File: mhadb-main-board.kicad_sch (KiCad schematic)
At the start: 9 parts, among them U1 ESP32-S3FN8

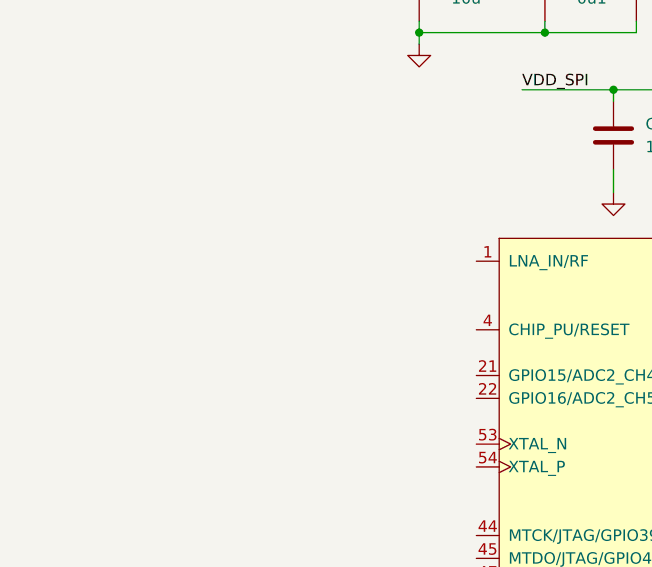
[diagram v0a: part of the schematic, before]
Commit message: schem: import 2.4GHZ rf circuit
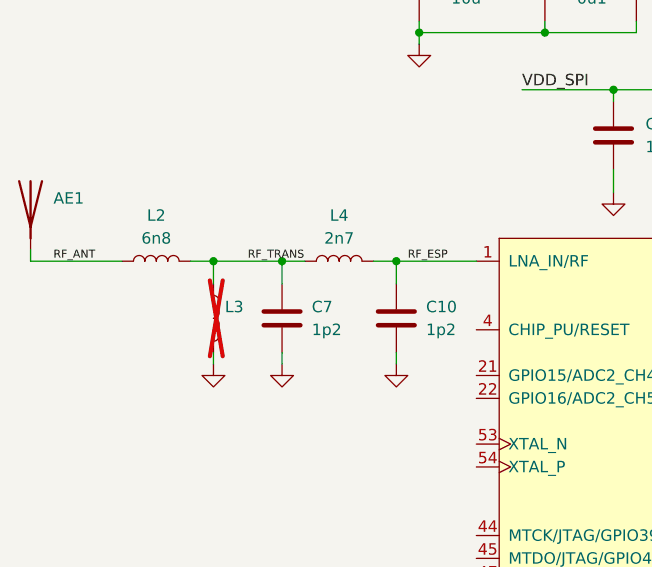
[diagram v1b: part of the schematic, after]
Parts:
- added AE1: Antenna, RF_Antenna:Johanson_2450AT18x100, symbol Device:Antenna
- added C10, C7: 1p2, Capacitor_SMD:C_0402_1005Metric, symbol Device:C
- added L2: 6n8, Inductor_SMD:L_0402_1005Metric, symbol Device:L
- added L3: L, Inductor_SMD:L_0402_1005Metric, symbol Device:L
- added L4: 2n7, Inductor_SMD:L_0402_1005Metric, symbol Device:L
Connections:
- net GND: now also C10.2, C7.2, L3.2
- net RF_ESP: now reaches U1.1 (LNA_IN/RF)
- net RF_ESP: now also C10.1, L4.2
- new net RF_ANT: AE1.1 (A), L2.1
- new net RF_TRANS: C7.1, L2.2, L3.1, L4.1

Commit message: schem: import reset circuit
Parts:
- added C1: 1u, Capacitor_SMD:C_0402_1005Metric, symbol Device:C
- added R1: 10k, Resistor_SMD:R_0402_1005Metric, symbol Device:R
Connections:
- net +3V3: now also R1.1
- net GND: now also C1.2
- net at U1.4 (CHIP_PU/RESET): now also C1.1, R1.2
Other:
- note added: "EN RC delay"
- moved on the sheet: AE1, C10, C7, L2, L3, L4

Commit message: schem: import HSE oscilator
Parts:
- added C2, C5: 12p, Capacitor_SMD:C_0402_1005Metric, symbol Device:C
- added L1: 24n, Inductor_SMD:L_0402_1005Metric, symbol Device:L
- added Y1: 48M, Crystal:Crystal_SMD_2016-4Pin_2.0x1.6mm, symbol Device:Crystal_GND24
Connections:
- net GND: now also C2.1, C5.2, Y1.2, Y1.4
- net XTAL_N: now reaches U1.53 (XTAL_N)
- net XTAL_N: now also C5.1, Y1.3
- net XTAL_P: now reaches U1.54 (XTAL_P)
- net XTAL_P: now also L1.1
- new net XTAL_PL: C2.2, L1.2, Y1.1
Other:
- note added: "HSE"

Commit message: schem: add BOOT pullup
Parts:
- added R9: 10k, Resistor_SMD:R_0402_1005Metric, symbol Device:R
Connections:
- net +3V3: now also R9.2
- net BOOT: now reaches U1.5 (GPIO0/BOOT)
- net BOOT: now also R9.1
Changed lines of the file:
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@@
 	(wire
 		(pts
+			(xy 240.03 73.66) (xy 245.11 73.66)
+		)
+		(stroke
+			(width 0)
+			(type default)
+		)
+	)
+	(wire
+		(pts
 			(xy 209.55 40.64) (xy 209.55 53.34)
 		)
@@
 	(wire
 		(pts
+			(xy 252.73 73.66) (xy 266.7 73.66)
+		)
+		(stroke
+			(width 0)
+			(type default)
+		)
+	)
+	(wire
+		(pts
 			(xy 227.33 40.64) (xy 227.33 41.91)
 		)
@@
 	(wire
 		(pts
+			(xy 266.7 72.39) (xy 266.7 73.66)
+		)
+		(stroke
+			(width 0)
+			(type default)
+		)
+	)
+	(wire
+		(pts
 			(xy 204.47 22.86) (xy 205.74 22.86)
 		)
@@
 		)
 	)
+	(label "BOOT"
+		(at 240.03 73.66 0)
+		(effects
+			(font
+				(size 1.27 1.27)
+			)
+			(justify left bottom)
+		)
+	)
 	(label "XTAL_N"
 		(at 45.72 181.61 180)
@@
 	(symbol
 		(lib_id "power:+3V3")
+		(at 266.7 72.39 0)
+		(unit 1)
+		(exclude_from_sim no)
+		(in_bom yes)
+		(on_board yes)
+		(dnp no)
+		(property "Reference" "#PWR032"
+			(at 266.7 76.2 0)
+			(effects
+				(font
+					(size 1.27 1.27)
+				)
+				(hide yes)
+			)
+		)
+		(property "Value" "+3V3"
+			(at 266.446 68.326 0)
+			(effects
+				(font
+					(size 1.27 1.27)
+				)
+			)
+		)
+		(property "Footprint" ""
+			(at 266.7 72.39 0)
+			(effects
+				(font
+					(size 1.27 1.27)
+				)
+				(hide yes)
+			)
+		)
+		(property "Datasheet" ""
+			(at 266.7 72.39 0)
+			(effects
+				(font
+					(size 1.27 1.27)
+				)
+				(hide yes)
+			)
+		)
+		(property "Description" "Power symbol creates a global label with name \"+3V3\""
+			(at 266.7 72.39 0)
+			(effects
+				(font
+					(size 1.27 1.27)
+				)
+				(hide yes)
+			)
+		)
+		(pin "1"
+		)
+		(instances
+			(project "mhadb-main-board"
+				(path "/108bdc05-5362-4b20-8d3b-92cc456652bf"
+					(reference "#PWR032")
+					(unit 1)
+				)
+			)
+		)
+	)
+	(symbol
+		(lib_id "power:+3V3")
 		(at 204.47 21.59 0)
 		(unit 1)
@@
 					(unit 1)
 				)
+			)
+		)
+	)
+	(symbol
+		(lib_id "Device:R")
+		(at 248.92 73.66 90)
+		(mirror x)
+		(unit 1)
+		(exclude_from_sim no)
+		(in_bom yes)
+		(on_board yes)
+		(dnp no)
+		(property "Reference" "R9"
+			(at 248.92 75.946 90)
+			(effects
+				(font
+					(size 1.27 1.27)
+				)
+			)
+		)
+		(property "Value" "10k"
+			(at 248.92 77.724 90)
+			(effects
+				(font
+					(size 1.27 1.27)
+				)
+			)
+		)
+		(property "Footprint" "Resistor_SMD:R_0402_1005Metric"
+			(at 248.92 71.882 90)
+			(effects
+				(font
+					(size 1.27 1.27)
+				)
+				(hide yes)
+			)
+		)
+		(property "Datasheet" "~"
+			(at 248.92 73.66 0)
+			(effects
+				(font
+					(size 1.27 1.27)
+				)
+				(hide yes)
+			)
+		)
+		(property "Description" "Resistor"
+			(at 248.92 73.66 0)
+			(effects
+				(font
+					(size 1.27 1.27)
+				)
+				(hide yes)
+			)
+		)
+		(property "Basic" "Y"
+			(at 248.92 73.66 90)
+			(effects
+				(font
+					(size 1.27 1.27)
+				)
+				(hide yes)
+			)
+		)
+		(property "JLCPCB Part #" "C25744"
+			(at 248.92 73.66 90)
+			(effects
+				(font
+					(size 1.27 1.27)
+				)
+				(hide yes)
+			)
+		)
+		(property "Manufacturer" "Uniroyal Elec"
+			(at 248.92 73.66 90)
+			(effects
+				(font
+					(size 1.27 1.27)
+				)
+				(hide yes)
+			)
+		)
+		(property "Manufacturer Part Number" "0402WGF1002TCE"
+			(at 248.92 73.66 90)
+			(effects
+				(font
+					(size 1.27 1.27)
+				)
+				(hide yes)
+			)
+		)
+		(pin "2"
+		)
+		(pin "1"
+		)
+		(instances
+			(project "mhadb-main-board"
+				(path "/108bdc05-5362-4b20-8d3b-92cc456652bf"
+					(reference "R9")
+					(unit 1)
+				)

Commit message: schem: import BOOT and CHIP_PU btns
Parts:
- added SW1, SW2: SW_Push, Button_Switch_SMD:SW_SPST_TS-1088-xR020, symbol Switch:SW_Push
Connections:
- net BOOT: now also SW1.2
- net GND: now also SW1.1, SW2.1
- net CHIP_PU: now reaches C1.1, R1.2, U1.4 (CHIP_PU/RESET)
- net CHIP_PU: now also SW2.2
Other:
- note added: "Buttons"

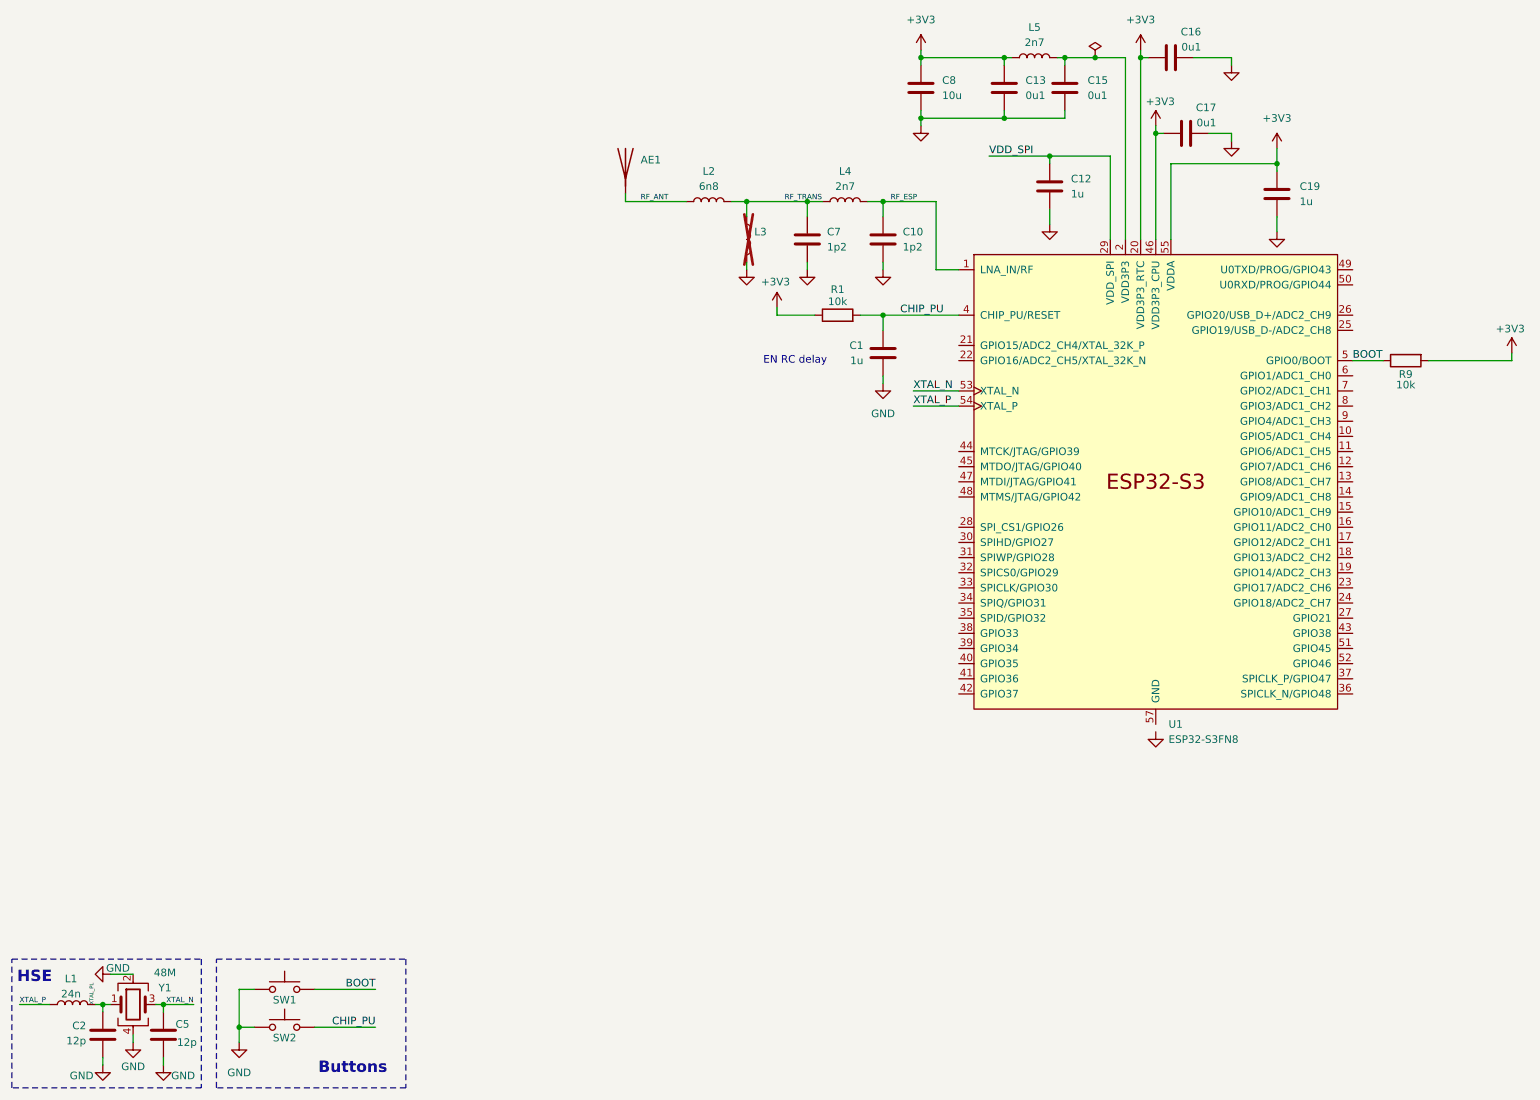
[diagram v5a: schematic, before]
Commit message: schem: add USB-C connector
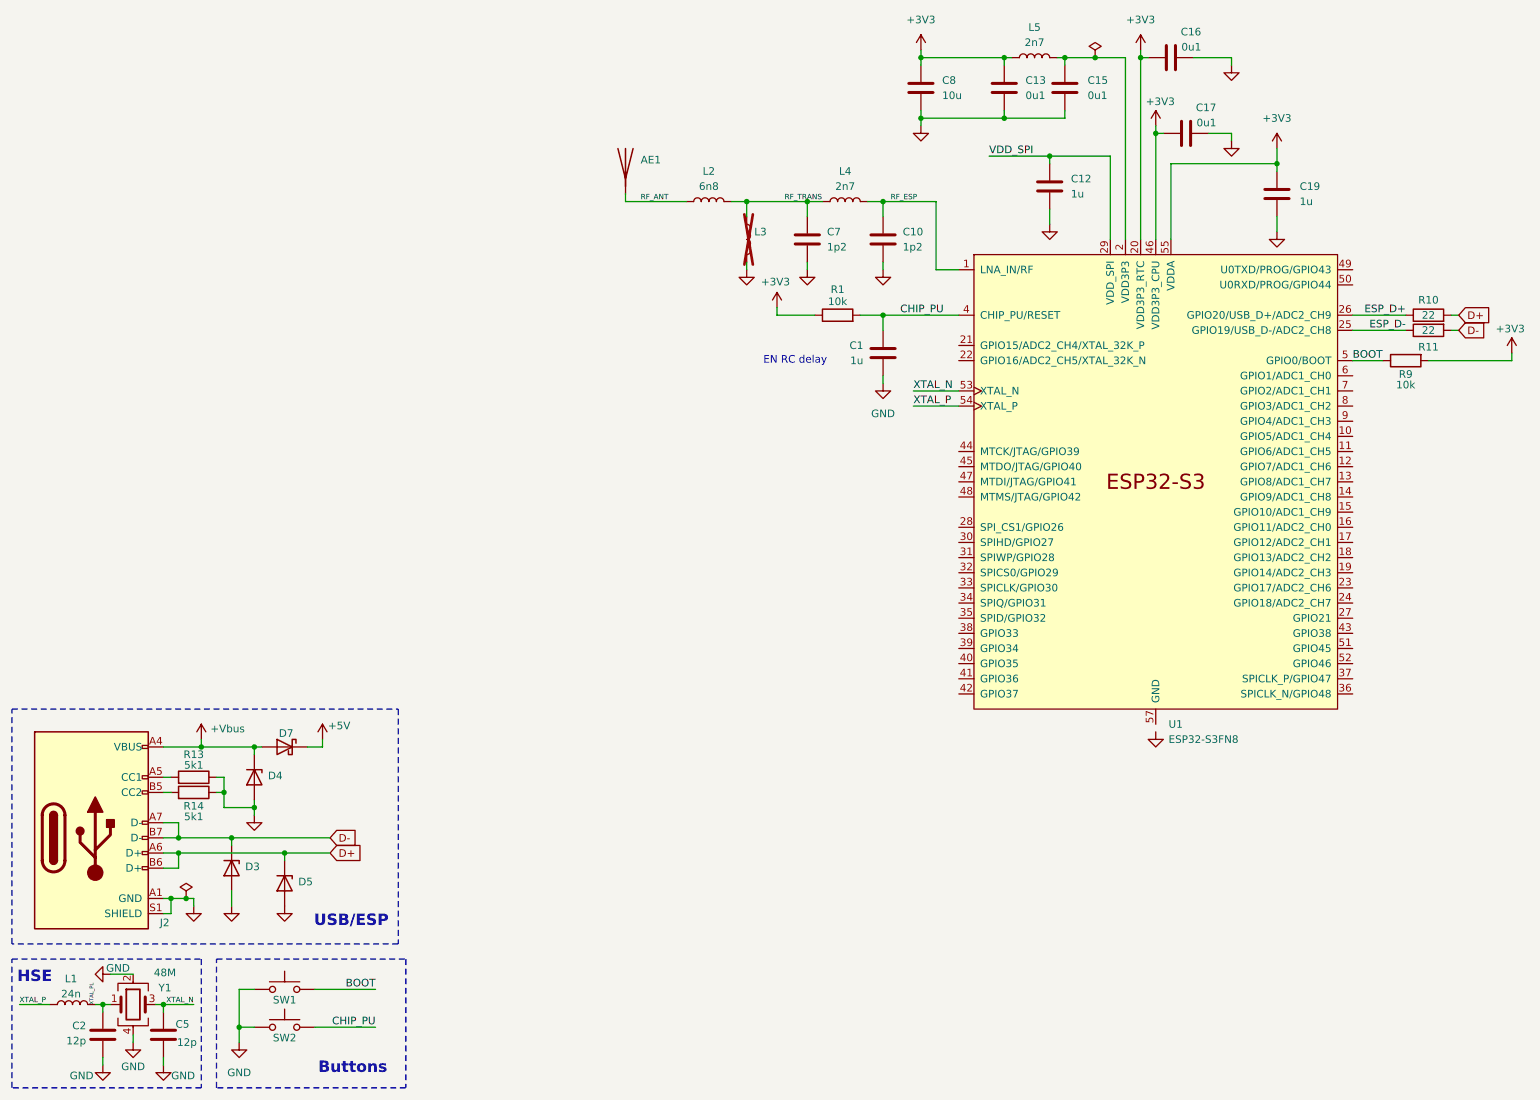
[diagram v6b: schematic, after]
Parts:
- added D3, D4, D5: H5VU10U, GLCS:Diode_DFN1006, symbol GLCS:H5VU10U
- added D7: D_Schottky, Diode_SMD:D_SMA, symbol Device:D_Schottky
- added J2: USB_C_Receptacle_USB2.0_14P, Connector_USB:USB_C_Receptacle_HRO_TYPE-C-31-M-12, symbol Connector:USB_C_Receptacle_USB2.0_14P
- added R10, R11: 22, Resistor_SMD:R_0402_1005Metric, symbol Device:R
- added R13, R14: 5k1, Resistor_SMD:R_0402_1005Metric, symbol Device:R
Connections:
- net GND: now also D3.2 (A), D4.2 (A), D5.2 (A), J2.A1 (GND), J2.A12 (GND), J2.B1 (GND), J2.B12 (GND), J2.S1 (SHIELD), R13.1, R14.1
- net ESP_D-: now reaches U1.25 (GPIO19/USB_D-/ADC2_CH8)
- net ESP_D-: now also R11.1
- net ESP_D+: now reaches U1.26 (GPIO20/USB_D+/ADC2_CH9)
- net ESP_D+: now also R10.1
- new net: J2.A5 (CC1), R13.2
- new net: J2.B5 (CC2), R14.2
- new net +5V: D7.1 (K)
- new net +Vbus: D4.1 (K), D7.2 (A), J2.A4 (VBUS), J2.A9 (VBUS), J2.B4 (VBUS), J2.B9 (VBUS)
- new net D+: D5.1 (K), J2.A6 (D+), J2.B6 (D+), R10.2
- new net D-: D3.1 (K), J2.A7 (D-), J2.B7 (D-), R11.2
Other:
- note added: "USB/ESP"

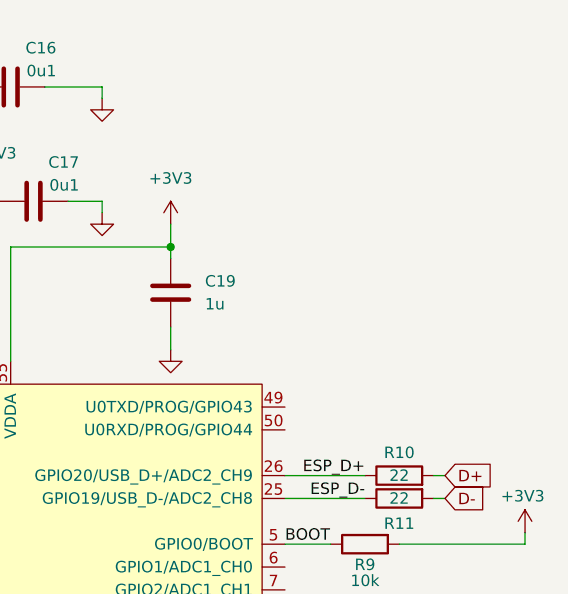
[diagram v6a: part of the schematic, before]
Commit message: schem: import UART connector
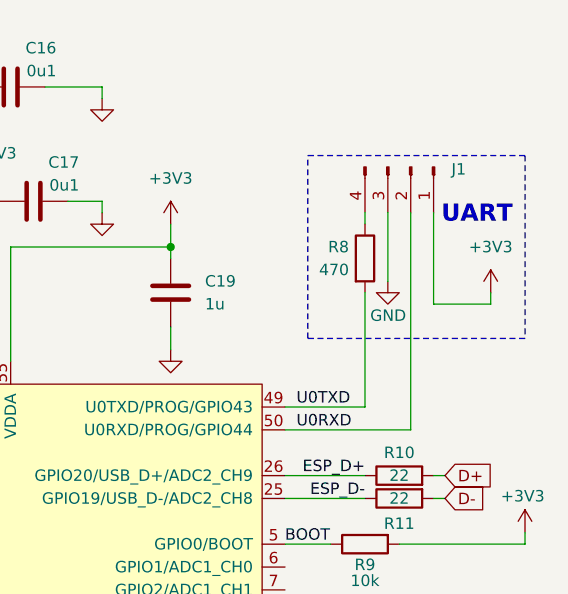
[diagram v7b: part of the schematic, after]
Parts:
- added J1: Conn_01x04_Pin, Connector_PinHeader_2.54mm:PinHeader_1x04_P2.54mm_Vertical, symbol Connector:Conn_01x04_Pin
- added R8: 470, Resistor_SMD:R_0402_1005Metric, symbol Device:R
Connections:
- net +3V3: now also J1.1 (Pin_1)
- net GND: now also J1.3 (Pin_3)
- net U0TXD: now reaches U1.49 (U0TXD/PROG/GPIO43)
- net U0TXD: now also R8.2
- net U0RXD: now reaches U1.50 (U0RXD/PROG/GPIO44)
- net U0RXD: now also J1.2 (Pin_2)
- new net: J1.4 (Pin_4), R8.1
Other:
- note added: "UART"

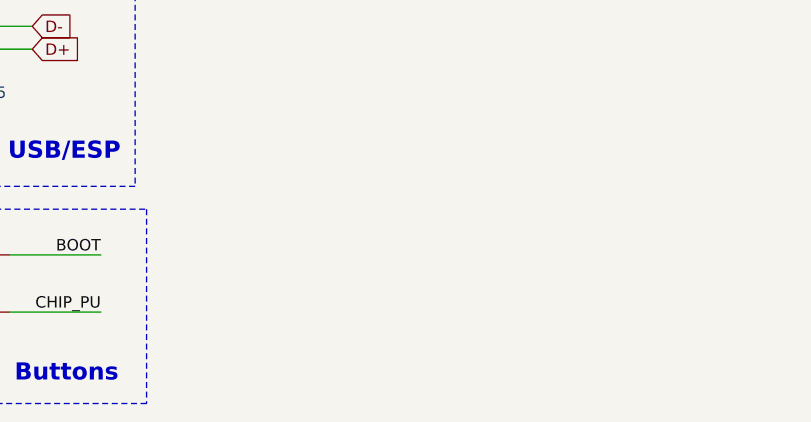
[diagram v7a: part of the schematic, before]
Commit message: schem: import LDL212 3V3 LDO
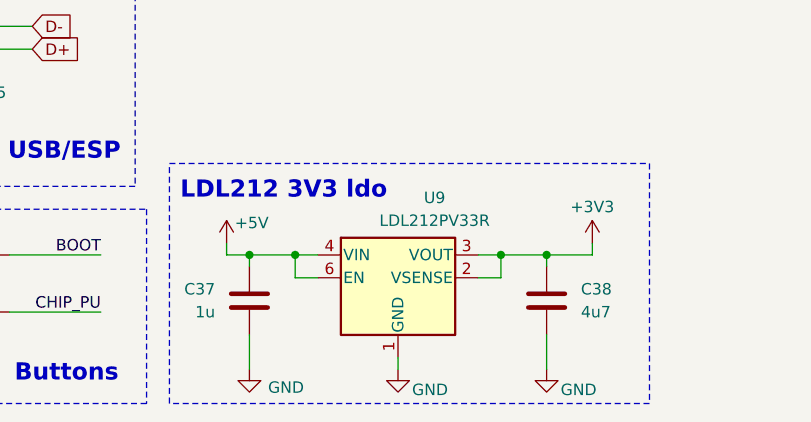
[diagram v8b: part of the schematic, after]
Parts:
- added C37: 1u, Capacitor_SMD:C_0402_1005Metric, symbol Device:C
- added C38: 4u7, Capacitor_SMD:C_0402_1005Metric, symbol Device:C
- added U9: LDL212PV33R, GLCS:DFN-6-1EP_2x2mm_P0.5mm_ST, symbol GLCS:LDL212PV33R
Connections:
- net +3V3: now also C38.1, U9.2 (VSENSE), U9.3 (VOUT)
- net +5V: now also C37.1, U9.4 (VIN), U9.6 (EN)
- net GND: now also C37.2, C38.2, U9.1 (GND)
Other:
- note added: "LDL212 3V3 ldo"
